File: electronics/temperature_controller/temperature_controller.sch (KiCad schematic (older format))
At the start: 31 parts, among them J1 Conn_01x03_Male, J2 Conn_01x03_Male, J3 Conn_01x03_Male, J4 Conn_01x03_Male, J5 Conn_01x03_Male, J6 Conn_01x03_Male, K1 RT44xxxx, K2 RT44xxxx, K3 ADW11, K4 ADW11, Q1 2N3904, Q2 2N3904, Q3 2N3904, Q4 2N3904, U1 MC7805CTG, U2 Pico

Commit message: finish board schematics
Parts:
- removed D1, D2, D3, D4: 1N4148TA, digikey-footprints:DO-35, symbol dk_Diodes-Rectifiers-Single:1N4148TA
- removed D5, D8: LED, LED_THT:LED_D3.0mm, symbol Device:LED
- removed J1, J2, J3: Conn_01x03_Male, TerminalBlock_Phoenix:TerminalBlock_Phoenix_MKDS-3-3-5.08_1x03_P5.08mm_Horizontal, symbol Connector:Conn_01x03_Male
- removed J5, J6: Conn_01x03_Male, Connector_PinHeader_2.54mm:PinHeader_1x03_P2.54mm_Vertical, symbol Connector:Conn_01x03_Male
- removed K1, K2: RT44xxxx, Relay_THT:Relay_DPST_Schrack-RT2-FormA_RM5mm, symbol Relay:RT44xxxx
- removed K3, K4: ADW11, Relay_THT:Relay_1P1T_NO_10x24x18.8mm_Panasonic_ADW11xxxxW_THT, symbol Relay:ADW11
- removed PS1: IRM-10-12, Converter_ACDC:Converter_ACDC_MeanWell_IRM-10-xx_THT, symbol Converter_ACDC:IRM-10-12
- removed Q1, Q2, Q3, Q4: 2N3904, digikey-footprints:TO-92-3, symbol dk_Transistors-Bipolar-BJT-Single:2N3904
- removed RV1, RV2: Varistor, Varistor:RV_Disc_D15.5mm_W4.2mm_P7.5mm, symbol Device:Varistor
- removed U1: MC7805CTG, digikey-footprints:TO-220-3, symbol dk_PMIC-Voltage-Regulators-Linear:MC7805CTG
- removed U2: Pico, MCU_RaspberryPi_and_Boards:RPi_Pico_SMD_TH, symbol MCU_RaspberryPi_and_Boards:Pico
- added D1, D4: LED, LED_THT:LED_D3.0mm, symbol Device:LED
- added D2, D3, D7, D8, D9: 1N5817, Diode_THT:D_DO-41_SOD81_P10.16mm_Horizontal, symbol Diode:1N5817
- added H1, H2, H3, H4: MountingHole, MountingHole:MountingHole_3.2mm_M3_Pad_TopBottom, symbol Mechanical:MountingHole
- added J1, J2, J4: SJ1-3523N, CUI_SJ1-3523N, symbol StereoJack:SJ1-3523N
- added J10, J11, J12, J13, J14, J15, J16, J18, J19, J20, J21, J5, J6, J7, J8, J9: 1217861-1, TE_1217861-1, symbol QuickConnectTab:1217861-1
- added J17, J30: Conn_01x03_Male, Connector_PinHeader_2.54mm:PinHeader_1x03_P2.54mm_Vertical, symbol Connector:Conn_01x03_Male
- added J22, J23: Conn_01x15_Male, Connector_PinHeader_2.54mm:PinHeader_1x15_P2.54mm_Vertical, symbol Connector:Conn_01x15_Male
- added J24, J25, J26, J27, J28, J29: TB006-508-02BE, CUI_TB006-508-02BE, symbol TerminalBlock:TB006-508-02BE
- added PS1: IRM-02-12, Converter_ACDC:Converter_ACDC_MeanWell_IRM-02-xx_THT, symbol Converter_ACDC:IRM-02-12
- added Q1, Q2, Q5, Q6: 2N3904, Package_TO_SOT_THT:TO-92_Inline, symbol Transistor_BJT:2N3904
- added Q3, Q4: IRF9Z34NPBF, Package_TO_SOT_THT:TO-220-3_Vertical, symbol Transistor_FET:IRF4905
- added R12, R13: 150, Resistor_SMD:R_0805_2012Metric_Pad1.20x1.40mm_HandSolder, symbol Device:R
- added R14, R15, R3, R4: 10k, Resistor_SMD:R_0805_2012Metric_Pad1.20x1.40mm_HandSolder, symbol Device:R
- added R16, R17, R5, R6, R7, R8: 1k, Resistor_SMD:R_0805_2012Metric_Pad1.20x1.40mm_HandSolder, symbol Device:R
- added R9: 4k7, Resistor_SMD:R_0805_2012Metric_Pad1.20x1.40mm_HandSolder, symbol Device:R
- added U1: MC7805CT-BPMS-ND, Package_TO_SOT_THT:TO-220-3_Vertical, symbol 5V_Regulator:MC7805CT-BPMS-ND
- added U2: NodeMCU1.0(ESP-12E), ESP8266:NodeMCU1.0(12-E), symbol ESP8266:NodeMCU1.0(ESP-12E)
- added U3: BOB-12009, CONV_BOB-12009, symbol BOBShifter:BOB-12009
- C1, C2: footprint Capacitor_THT:C_Rect_L18.0mm_W9.0mm_P15.00mm_FKS3_FKP3 -> Capacitor_THT:C_Disc_D8.0mm_W2.5mm_P5.00mm
- R1, R2: value R -> 150; footprint Resistor_THT:R_Axial_DIN0516_L15.5mm_D5.0mm_P25.40mm_Horizontal -> Resistor_SMD:R_0805_2012Metric_Pad1.20x1.40mm_HandSolder
- renumbered D7 to D5, J4 to J3
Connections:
- net +12V: now also C2.1, D1.2 (A), D4.2 (A), D7.1 (K), D8.1 (K), J18.1, J18.2, J20.1, J20.2, J27.1, J28.1, J29.1, J30.3 (Pin_3), PS1.4 (+Vo), Q3.3 (S), Q4.3 (S), R7.2, R8.2, U1.1 (IN)
- net +5V: now also D9.1 (K), J1.2, J2.2, J22.15 (Pin_15), J24.1, J25.1, J26.1, J30.1 (Pin_1), J4.2, R9.1, U2.15 (VIN)
- net COOL: now also J23.8 (Pin_8), R13.2, U2.23 (D5(GPIO14))
- net FAN1: now also R1.2, J23.5 (Pin_5), U2.26 (D4(GPIO2))
- net FAN2: now also R2.2, J23.11 (Pin_11), U2.20 (D8(GPIO15))
- net GND: now also C1.2, C2.2, D2.2 (A), D3.2 (A), J1.1, J17.1 (Pin_1), J2.1, J22.10 (Pin_10), J22.14 (Pin_14), J23.14 (Pin_14), J23.7 (Pin_7), J24.2, J25.2, J26.2, J27.2, J28.2, J29.2, J4.1, PS1.3 (-Vo), Q1.1 (E), Q2.1 (E), Q5.1 (E), Q6.1 (E), R14.1, R15.1, R3.1, R4.1, U1.2 (GND), U2.10 (GND), U2.14 (GND), U2.17 (GND), U2.24 (GND), U3.GND_1 (GND), U3.GND_2 (GND)
- net HEAT: now also J23.1 (Pin_1), R12.2, U2.30 (D0(GPIO16))
- net LIVE: now also J13.1, J13.2, J14.1, J14.2, J15.1, J15.2, J16.1, J16.2, PS1.2 (AC/L)
- net NEUTRAL: now also J10.1, J10.2, J11.1, J11.2, J12.1, J12.2, J9.1, J9.2, PS1.1 (AC/N)
- net at D6.1 (K): now also R17.1
- net at C1.1: now also D9.2 (A), U1.3 (OUT)
- net at J3.2 (Pin_2): now also D2.1 (K), Q3.2 (D)
- net at R2.1: now also Q2.2 (B), R4.2; no longer C2.2
- net at R1.1: now also Q1.2 (B), R3.2; no longer C1.2
- net at D5.1 (K): now also R5.1
- new net: J22.1 (Pin_1), U2.1 (A0(ADC0))
- new net: J22.11 (Pin_11), U2.11 (3.3V)
- new net: J22.12 (Pin_12), U2.12 (EN)
- new net: J22.13 (Pin_13), U2.13 (RST)
- new net: J23.15 (Pin_15), U2.16 (3.3V)
- new net: J23.13 (Pin_13), U2.18 (TX(GPIO1))
- new net: J23.12 (Pin_12), U2.19 (RX(DPIO3))
- new net: J22.2 (Pin_2), U2.2 (RSV)
- new net: J23.10 (Pin_10), U2.21 (D7(GPIO13))
- new net: J23.6 (Pin_6), U2.25 (3.3V), U3.LV
- new net: J23.4 (Pin_4), U2.27 (D3(GPIO0)), U3.LV3
- new net: J23.3 (Pin_3), U2.28 (D2(GPIO4)), U3.LV2
- new net: J23.2 (Pin_2), U2.29 (D1(GPIO5)), U3.LV1
- new net: J22.3 (Pin_3), U2.3 (RSV)
- new net: J22.4 (Pin_4), U2.4 (SD3(GPIO10))
- new net: J22.5 (Pin_5), U2.5 (SD2(GPIO9))
- new net: J22.6 (Pin_6), U2.6 (SD1(MOSI))
- new net: J22.7 (Pin_7), U2.7 (CMD(CS))
- new net: J22.8 (Pin_8), U2.8 (SDO(MISO))
- new net: J22.9 (Pin_9), U2.9 (CLK(SCLK))
- new net: Q1.3 (C), Q3.1 (G), R5.2, R7.1
- new net: D4.1 (K), R16.1
- new net: D7.2 (A), J19.1, J19.2, Q5.3 (C), R16.2
- new net: Q5.2 (B), R12.1, R14.2
- new net: D1.1 (K), R6.1
- new net: Q2.3 (C), Q4.1 (G), R6.2, R8.1
- new net: D3.1 (K), J17.2 (Pin_2), Q4.2 (D)
- new net: D8.2 (A), J21.1, J21.2, Q6.3 (C), R17.2
- new net: Q6.2 (B), R13.1, R15.2
- new net: J30.2 (Pin_2), U3.HV
- new net EARTH: J5.1, J5.2, J6.1, J6.2, J7.1, J7.2, J8.1, J8.2
- new net ONEWIRE: J1.3, J2.3, J23.9 (Pin_9), J4.3, R9.2, U2.22 (D6(GPIO12))
- no-connect marks 29 -> 8
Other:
- moved on the sheet: D5, J3

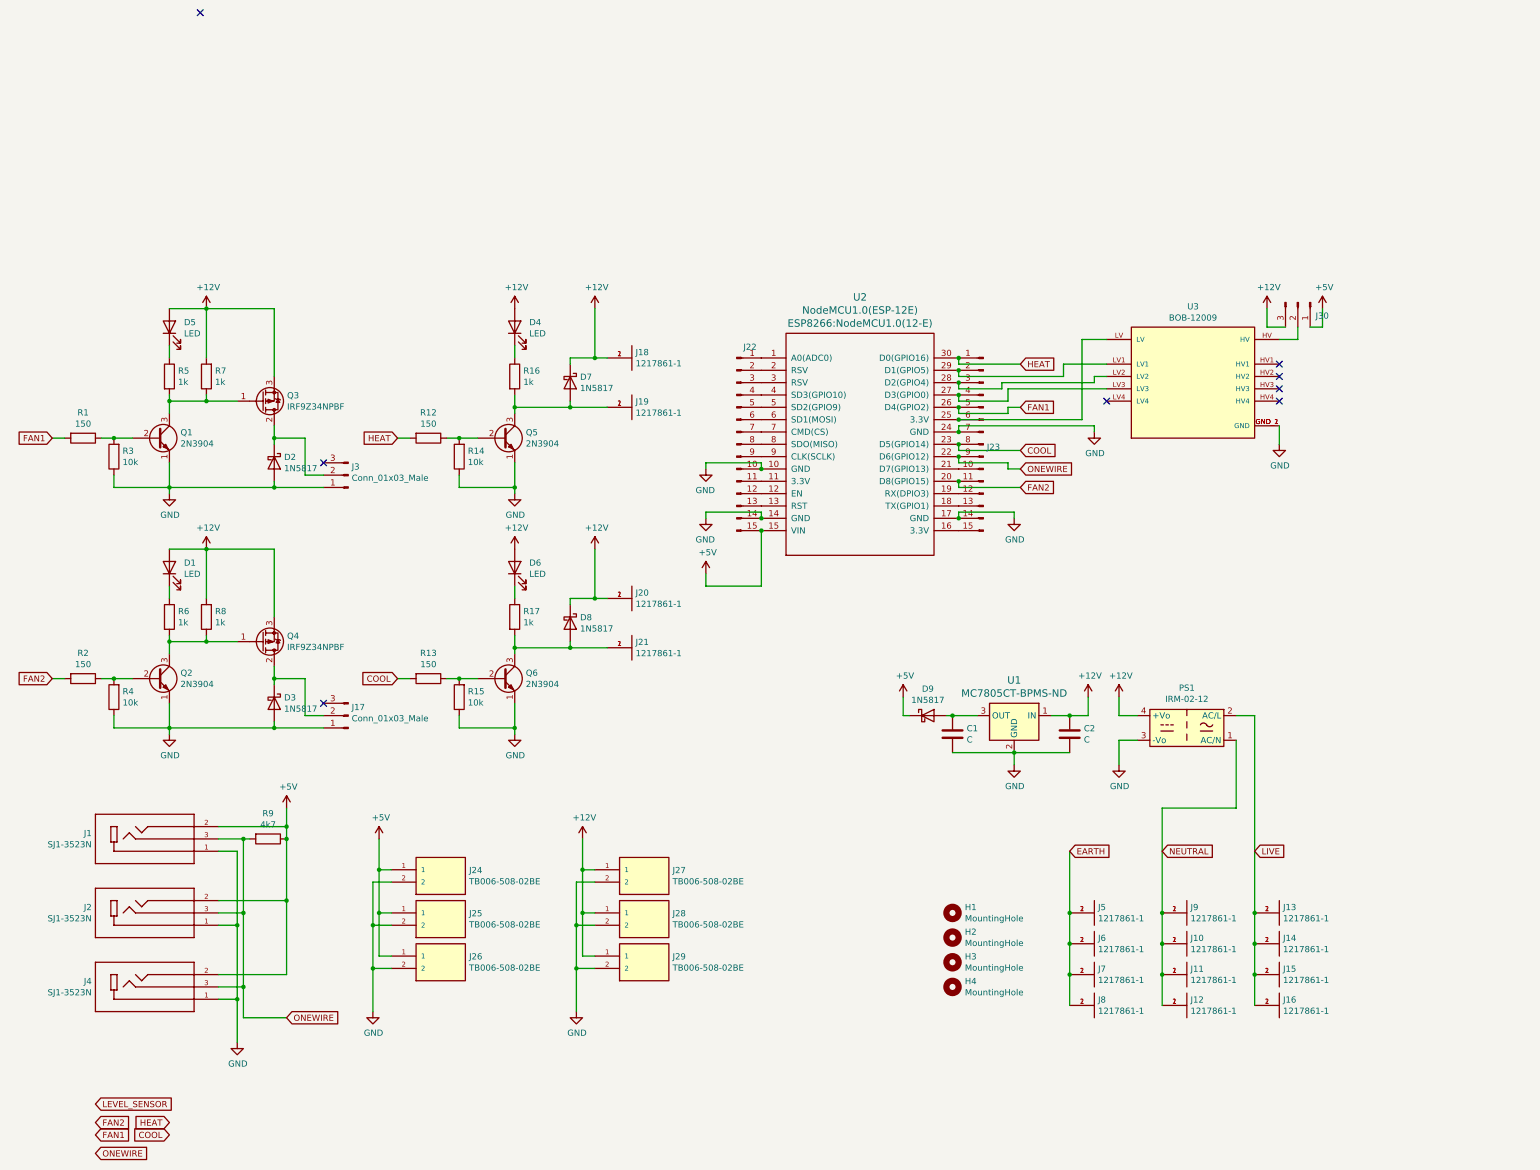
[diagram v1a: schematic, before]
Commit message: update footprints, schematic and start board layout
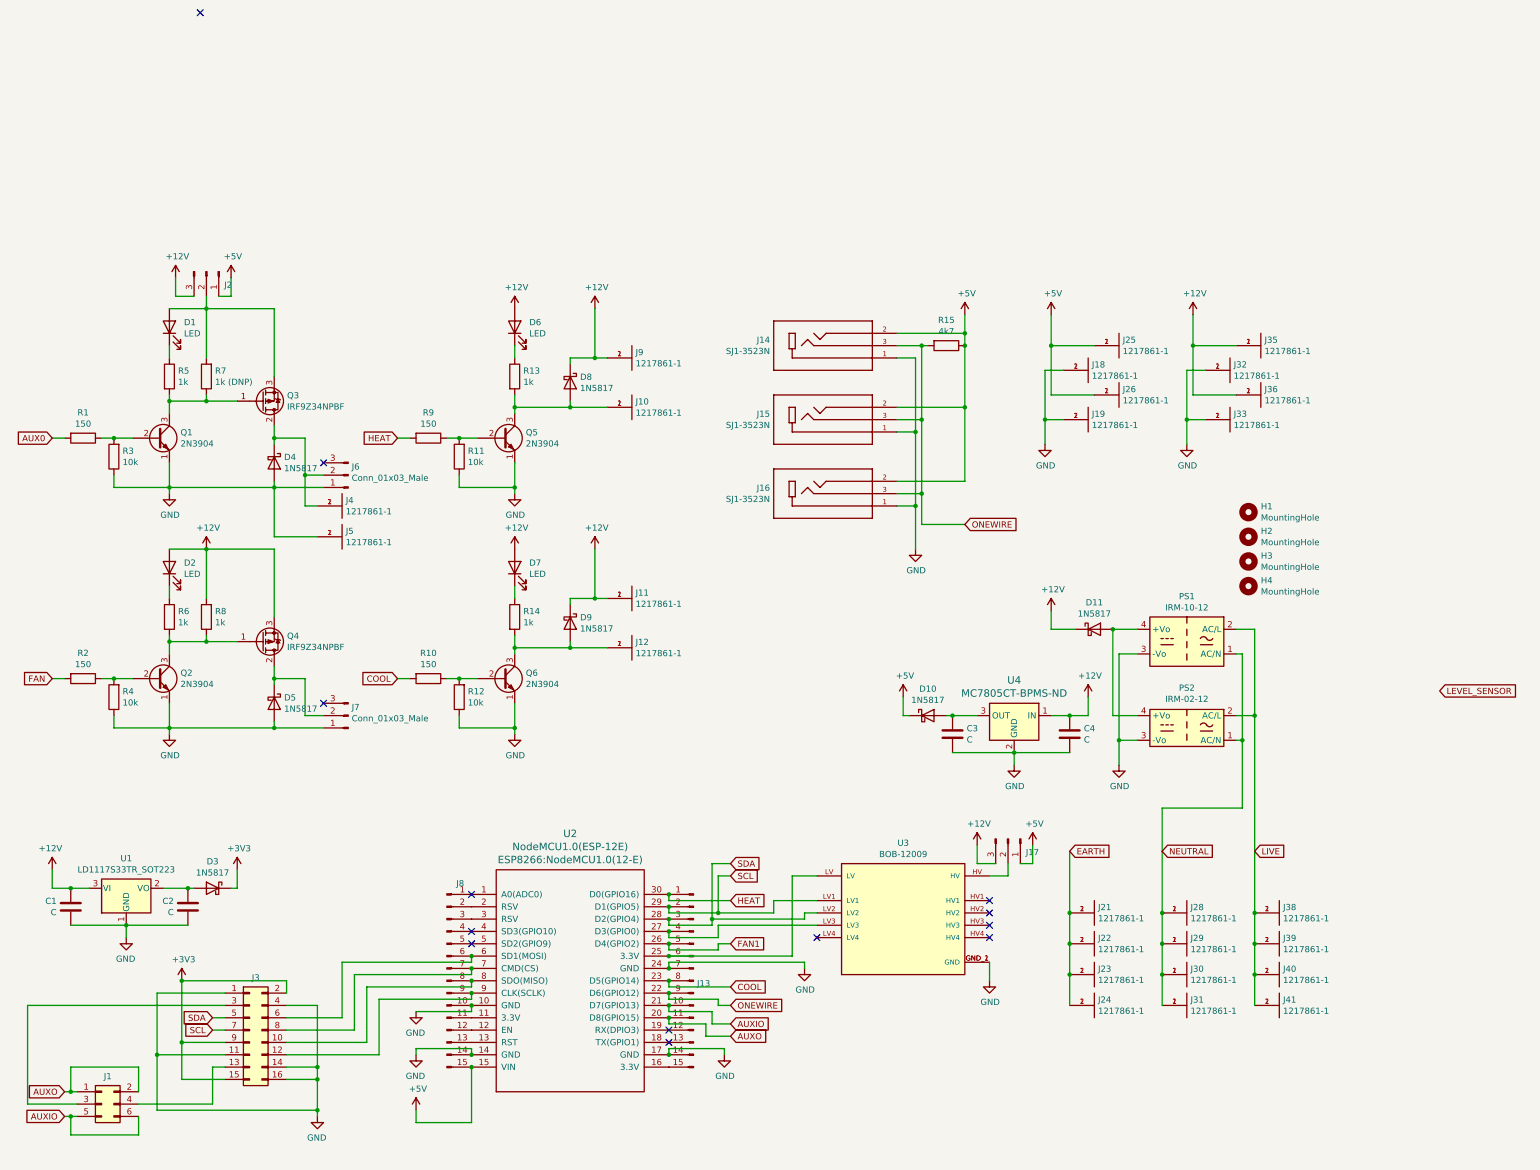
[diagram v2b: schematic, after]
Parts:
- removed J24, J25, J26, J27, J28, J29: TB006-508-02BE, CUI_TB006-508-02BE, symbol TerminalBlock:TB006-508-02BE
- added C1, C2: C, Capacitor_THT:C_Disc_D8.0mm_W2.5mm_P5.00mm, symbol Device:C
- added D11, D3: 1N5817, Diode_THT:D_DO-41_SOD81_P10.16mm_Horizontal, symbol Diode:1N5817
- added J1: Conn_02x03_Odd_Even, Connector_PinHeader_2.54mm:PinHeader_2x03_P2.54mm_Vertical, symbol Connector_Generic:Conn_02x03_Odd_Even
- added J18, J19, J25, J26, J32, J33, J35, J36, J4, J5: 1217861-1, TE_1217861-1, symbol QuickConnectTab:1217861-1
- added J2: Conn_01x03_Male, Connector_PinHeader_2.54mm:PinHeader_1x03_P2.54mm_Vertical, symbol Connector:Conn_01x03_Male
- added J3: Conn_02x08_Odd_Even, Connector_PinHeader_2.54mm:PinHeader_2x08_P2.54mm_Vertical, symbol Connector_Generic:Conn_02x08_Odd_Even
- added PS1: IRM-10-12, Converter_ACDC:Converter_ACDC_MeanWell_IRM-10-xx_THT, symbol Converter_ACDC:IRM-10-12
- added U1: LD1117S33TR_SOT223, Package_TO_SOT_SMD:SOT-223-3_TabPin2, symbol Regulator_Linear:LD1117S33TR_SOT223
- R7: value 1k -> 1k (DNP)
- renumbered C1 to C3, C2 to C4, D5 to D1, D9 to D10, D1 to D2, D2 to D4, D3 to D5, D4 to D6, D6 to D7, D7 to D8, D8 to D9, J19 to J10, J20 to J11, J21 to J12, J23 to J13, J1 to J14, J2 to J15, J4 to J16, J30 to J17, J5 to J21, J6 to J22, J7 to J23, J8 to J24, J9 to J28, J10 to J29, J11 to J30, J12 to J31, J13 to J38, J14 to J39, J15 to J40, J16 to J41, J3 to J6, J17 to J7, J22 to J8, J18 to J9, PS1 to PS2, R13 to R10, R14 to R11, R15 to R12, R16 to R13, R17 to R14, R9 to R15, R12 to R9, U1 to U4
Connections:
- net +12V: now also C1.1, D11.1 (K), J2.3 (Pin_3), J35.1, J35.2, J36.1, J36.2, U1.3 (VI); no longer D1.2 (A), PS2.4 (+Vo), Q3.3 (S), R7.2
- net +5V: now also J2.1 (Pin_1), J25.1, J25.2, J26.1, J26.2
- net FAN1: no longer R1.2
- net GND: now also C1.2, C2.2, J18.1, J18.2, J19.1, J19.2, J3.1 (Pin_1), J3.11 (Pin_11), J3.14 (Pin_14), J3.16 (Pin_16), J3.4 (Pin_4), J32.1, J32.2, J33.1, J33.2, J5.1, J5.2, PS1.3 (-Vo), U1.1 (GND)
- net LIVE: now also PS1.2 (AC/L)
- net NEUTRAL: now also PS1.1 (AC/N)
- net at D4.1 (K), J6.2 (Pin_2), Q3.2 (D): now also J4.1, J4.2
- net AUXIO: now reaches J13.10 (Pin_10), U2.21 (D7(GPIO13))
- net AUXIO: now also J1.5 (Pin_5), J1.6 (Pin_6)
- net SDA: now reaches J13.3 (Pin_3), U2.28 (D2(GPIO4)), U3.LV2
- net SDA: now also J3.5 (Pin_5)
- net SCL: now reaches J13.2 (Pin_2), U2.29 (D1(GPIO5)), U3.LV1
- net SCL: now also J3.7 (Pin_7)
- net at J8.6 (Pin_6), U2.6 (SD1(MOSI)): now also J3.6 (Pin_6)
- net at J8.7 (Pin_7), U2.7 (CMD(CS)): now also J3.8 (Pin_8)
- net at J8.8 (Pin_8), U2.8 (SDO(MISO)): now also J3.10 (Pin_10)
- net at J8.9 (Pin_9), U2.9 (CLK(SCLK)): now also J3.12 (Pin_12)
- net FAN2 renamed AUXO
- net AUXO: now also J1.1 (Pin_1), J1.2 (Pin_2); no longer R2.2
- new net: D1.2 (A), J2.2 (Pin_2), Q3.3 (S), R7.2
- new net: D11.2 (A), PS1.4 (+Vo), PS2.4 (+Vo)
- new net: J1.4 (Pin_4), J3.13 (Pin_13)
- new net: J1.3 (Pin_3), J3.3 (Pin_3)
- new net: C2.1, D3.2 (A), U1.2 (VO)
- new net +3V3: D3.1 (K), J3.15 (Pin_15), J3.2 (Pin_2), J3.9 (Pin_9)
- new net AUX0: R1.2
- new net FAN: R2.2
- no-connect marks 8 -> 13
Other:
- moved on the sheet: H1, H2, H3, H4, J13, J14, J15, J16, J17, J8, R15, U2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

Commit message: finished layout move to bluetooth shield
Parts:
- removed C1, C2: C, Capacitor_THT:C_Disc_D8.0mm_W2.5mm_P5.00mm, symbol Device:C
- removed D10, D11, D3, D4, D5, D8, D9: 1N5817, Diode_THT:D_DO-41_SOD81_P10.16mm_Horizontal, symbol Diode:1N5817
- removed J13, J8: Conn_01x15_Male, Connector_PinHeader_2.54mm:PinHeader_1x15_P2.54mm_Vertical, symbol Connector:Conn_01x15_Male
- removed J18, J19: 1217861-1, TE_1217861-1, symbol QuickConnectTab:1217861-1
- removed U1: LD1117S33TR_SOT223, Package_TO_SOT_SMD:SOT-223-3_TabPin2, symbol Regulator_Linear:LD1117S33TR_SOT223
- added D10, D3, D4, D5, D8, D9: ‎DSS13UTR‎, ProjectComponents:D_SOD-123F, symbol Device:D_Schottky
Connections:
- net AUX0 is gone; now on net AUXO: R1.2
- net FAN1 is gone; now on net FAN: U2.26 (D4(GPIO2))
- net +12V: now also J3.14 (Pin_14), J3.2 (Pin_2), D10.1 (K), D5.1 (K), D8.1 (K)
- net +5V: now also J3.15 (Pin_15), J3.9 (Pin_9), D9.1 (K)
- net GND: now also D3.2 (A), D4.2 (A); no longer J3.14 (Pin_14)
- net at J4.1, J4.2, J6.2 (Pin_2)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: now also D3.1 (K)
- net at PS1.4 (+Vo), PS2.4 (+Vo): now also D10.2 (A)
- net MOSI: now reaches J3.6 (Pin_6), U2.6 (SD1(MOSI))
- net CS: now reaches J3.8 (Pin_8), U2.7 (CMD(CS))
- net MISO: now reaches J3.10 (Pin_10), U2.8 (SDO(MISO))
- net SCLK: now reaches J3.12 (Pin_12), U2.9 (CLK(SCLK))
- net at J10.1, J10.2, Q5.3 (C)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: now also D5.2 (A)
- net at J7.2 (Pin_2), Q4.2 (D): now also D4.1 (K)
- net at J12.1, J12.2, Q6.3 (C)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: now also D8.2 (A)
- net at C3.1, U4.3 (OUT): now also D9.2 (A)
- removed net +3V3: J3.15 (Pin_15), J3.2 (Pin_2), J3.9 (Pin_9)
- no-connect marks 13 -> 19
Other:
- moved on the sheet: J1, J3

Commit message: Updating layouts for better shield addition
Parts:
- R7: value 1k (DNP) -> DNP
- R8: value 1k -> DNP
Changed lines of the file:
@@
 P 2000 1300
 F 0 "R7" H 1930 1254 50  0000 R CNN
-F 1 "1k (DNP)" H 1930 1345 50  0000 R CNN
+F 1 "DNP" H 1930 1345 50  0000 R CNN
 F 2 "Resistor_SMD:R_0805_2012Metric_Pad1.20x1.40mm_HandSolder" V 1930 1300 50  0001 C CNN
 F 3 "~" H 2000 1300 50  0001 C CNN
@@
 P 2000 3250
 F 0 "R8" H 1930 3204 50  0000 R CNN
-F 1 "1k" H 1930 3295 50  0000 R CNN
+F 1 "DNP" H 1930 3295 50  0000 R CNN
 F 2 "Resistor_SMD:R_0805_2012Metric_Pad1.20x1.40mm_HandSolder" V 1930 3250 50  0001 C CNN
 F 3 "~" H 2000 3250 50  0001 C CNN
